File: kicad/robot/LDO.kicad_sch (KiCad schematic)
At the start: 17 parts, among them U14 MAX77642ANA+

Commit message: WARNING more BOM batch edits
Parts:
- R52: Manufacturer (none) -> Stackpole Electronics; Part Number (none) -> RMCF0603FT768K
- R53: Manufacturer (none) -> Panasonic; Part Number (none) -> ERJ-1GEF1133C
- R54: Manufacturer (none) -> Stackpole Electronics; Part Number (none) -> RMCF0603FT28K0
- R55: Manufacturer (none) -> Stackpole Electronics; Part Number (none) -> RMCF0603FT14K0
- U14: Part Number (none) -> MAX77642ANA+
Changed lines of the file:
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@@
     )
     (property "Description" "%1" (id 4) (at 72.39 121.92 0))
+    (property "Manufacturer" "Panasonic" (id 5) (at 68.58 118.11 0)
+      (effects (font (size 1.27 1.27)) hide)
+    )
+    (property "Part Number" "ERJ-1GEF1133C" (id 6) (at 68.58 118.11 0)
+      (effects (font (size 1.27 1.27)) hide)
+    )
     (pin "1")
     (pin "2")
@@
     (property "temperature range low" "-40°C" (id 30) (at 93.98 -5.08 0)
       (effects (font (size 1.27 1.27)) (justify left) hide)
+    )
+    (property "Part Number" "MAX77642ANA+" (id 31) (at 93.98 76.2 0)
+      (effects (font (size 1.27 1.27)) hide)
     )
     (pin "A1")
@@
     )
     (property "Description" "%1" (id 4) (at 82.55 121.92 0))
+    (property "Manufacturer" "Stackpole Electronics" (id 5) (at 78.74 118.11 0)
+      (effects (font (size 1.27 1.27)) hide)
+    )
+    (property "Part Number" "RMCF0603FT28K0" (id 6) (at 78.74 118.11 0)
+      (effects (font (size 1.27 1.27)) hide)
+    )
     (pin "1")
     (pin "2")
@@
     )
     (property "Description" "%1" (id 4) (at 92.71 121.92 0))
+    (property "Manufacturer" "Stackpole Electronics" (id 5) (at 88.9 118.11 0)
+      (effects (font (size 1.27 1.27)) hide)
+    )
+    (property "Part Number" "RMCF0603FT14K0" (id 6) (at 88.9 118.11 0)
+      (effects (font (size 1.27 1.27)) hide)
+    )
     (pin "1")
     (pin "2")
@@
     )
     (property "Description" "%1" (id 4) (at 62.23 121.92 0))
-    (pin "1")
-    (pin "2")
+    (property "Manufacturer" "Stackpole Electronics" (id 5) (at 58.42 118.11 0)
+      (effects (font (size 1.27 1.27)) hide)
+    )
+    (property "Part Number" "RMCF0603FT768K" (id 6) (at 58.42 118.11 0)
+      (effects (font (size 1.27 1.27)) hide)
+    )
+    (pin "1")
+    (pin "2")

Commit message: Added stock counts to parts I have
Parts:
- U14: Stock (none) -> 25
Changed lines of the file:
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@@
+      (effects (font (size 1.27 1.27)) hide)
+    )
+    (property "Stock" "25" (id 32) (at 93.98 76.2 0)
       (effects (font (size 1.27 1.27)) hide)
     )

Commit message: Batch BOM edits adding manufactuer and part numbers only
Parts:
- U14: Manufacturer (none) -> Maxim; manufacturer Maxim -> (none)
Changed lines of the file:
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@@
       (effects (font (size 1.27 1.27)) (justify left) hide)
     )
-    (property "manufacturer" "Maxim" (id 16) (at 93.98 30.48 0)
+    (property "manufacturer" "" (id 16) (at 93.98 30.48 0)
       (effects (font (size 1.27 1.27)) (justify left) hide)
     )
@@
       (effects (font (size 1.27 1.27)) hide)
     )
+    (property "Manufacturer" "Maxim" (id 33) (at 93.98 76.2 0)
+      (effects (font (size 1.27 1.27)) hide)
+    )

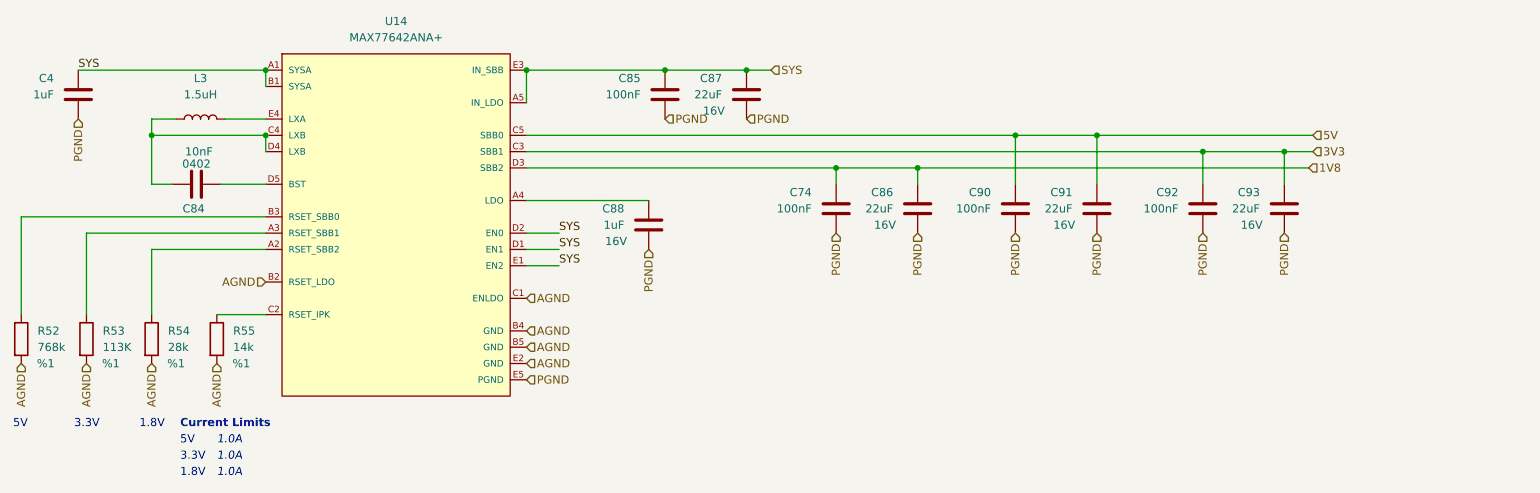
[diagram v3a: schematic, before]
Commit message: bulk BOM edits. Mainly dealing with cap voltage ratings and part selection
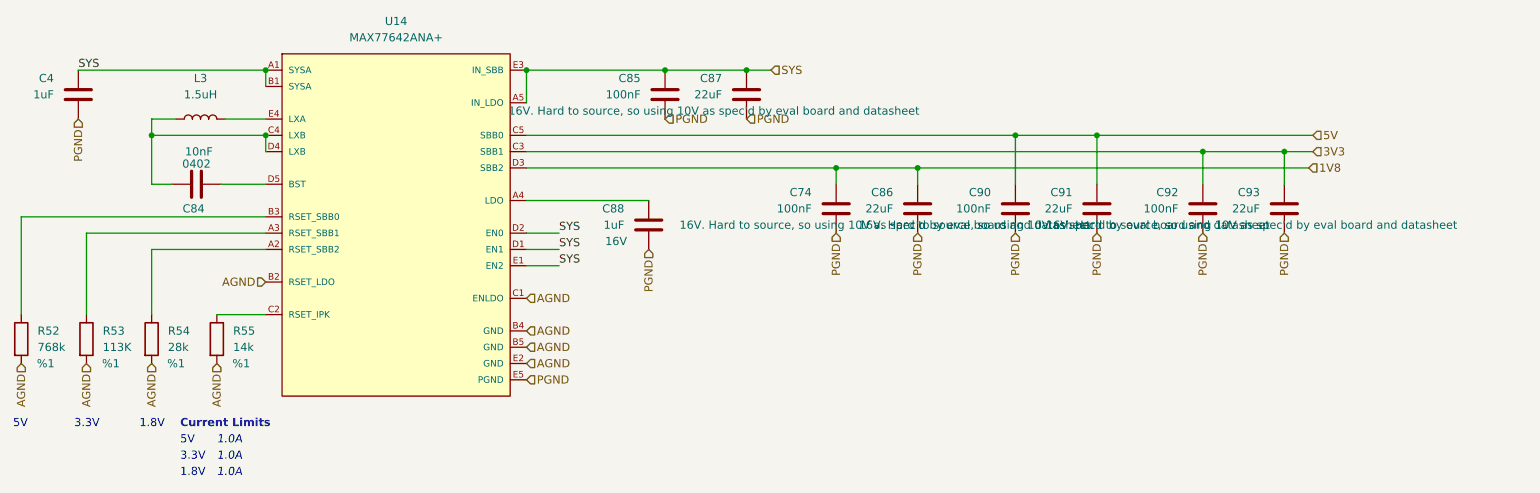
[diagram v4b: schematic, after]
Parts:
- C4: Manufacturer (none) -> Samsung; Part Number (none) -> CL10A105KQ8NNNC
- C74, C85, C90, C92: Manufacturer (none) -> Samsung; Part Number (none) -> CL10B104KB8NNWC
- C84: Manufacturer (none) -> Samsung; Part Number (none) -> CL05B103KA5NNNC
- C86, C87, C91, C93: Manufacturer (none) -> Samsung; Part Number (none) -> CL10A226MP8NUNE
- C88: Manufacturer (none) -> Samsung; Part Number (none) -> CL10A105KA8NNNC
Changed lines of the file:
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@@
       (effects (font (size 1.27 1.27)) hide)
     )
-    (property "Description" "16V" (id 4) (at 250.19 100.33 0))
+    (property "Description" "16V. Hard to source, so using 10V as spec'd by eval board and datasheet" (id 4) (at 250.19 100.33 0))
+    (property "Manufacturer" "Samsung" (id 5) (at 255.27 97.79 0)
+      (effects (font (size 1.27 1.27)) hide)
+    )
+    (property "Part Number" "CL10A226MP8NUNE" (id 6) (at 255.27 97.79 0)
+      (effects (font (size 1.27 1.27)) hide)
+    )
     (pin "1")
     (pin "2")
@@
     )
     (property "Description" "16V" (id 4) (at 151.13 102.87 0))
+    (property "Manufacturer" "Samsung" (id 5) (at 156.21 100.33 0)
+      (effects (font (size 1.27 1.27)) hide)
+    )
+    (property "Part Number" "CL10A105KA8NNNC" (id 6) (at 156.21 100.33 0)
+      (effects (font (size 1.27 1.27)) hide)
+    )
     (pin "1")
     (pin "2")
@@
       (effects (font (size 1.27 1.27)) hide)
     )
-    (property "Description" "16V" (id 4) (at 166.37 82.55 0))
+    (property "Description" "16V. Hard to source, so using 10V as spec'd by eval board and datasheet" (id 4) (at 166.37 82.55 0))
+    (property "Manufacturer" "Samsung" (id 5) (at 171.45 80.01 0)
+      (effects (font (size 1.27 1.27)) hide)
+    )
+    (property "Part Number" "CL10A226MP8NUNE" (id 6) (at 171.45 80.01 0)
+      (effects (font (size 1.27 1.27)) hide)
+    )
     (pin "1")
     (pin "2")
@@
       (effects (font (size 1.27 1.27)) hide)
     )
-    (property "Description" "16V" (id 4) (at 193.04 100.33 0))
+    (property "Description" "16V. Hard to source, so using 10V as spec'd by eval board and datasheet" (id 4) (at 193.04 100.33 0))
+    (property "Manufacturer" "Samsung" (id 5) (at 198.12 97.79 0)
+      (effects (font (size 1.27 1.27)) hide)
+    )
+    (property "Part Number" "CL10A226MP8NUNE" (id 6) (at 198.12 97.79 0)
+      (effects (font (size 1.27 1.27)) hide)
+    )
     (pin "1")
     (pin "2")
@@
     )
     (property "Description" "" (id 4) (at 180.34 100.33 0))
+    (property "Manufacturer" "Samsung" (id 5) (at 185.42 97.79 0)
+      (effects (font (size 1.27 1.27)) hide)
+    )
+    (property "Part Number" "CL10B104KB8NNWC" (id 6) (at 185.42 97.79 0)
+      (effects (font (size 1.27 1.27)) hide)
+    )
     (pin "1")
     (pin "2")
@@
     )
     (property "Description" "" (id 4) (at 153.67 82.55 0))
+    (property "Manufacturer" "Samsung" (id 5) (at 158.75 80.01 0)
+      (effects (font (size 1.27 1.27)) hide)
+    )
+    (property "Part Number" "CL10B104KB8NNWC" (id 6) (at 158.75 80.01 0)
+      (effects (font (size 1.27 1.27)) hide)
+    )
     (pin "1")
     (pin "2")
@@
     )
     (property "Description" "" (id 4) (at 62.23 82.55 0))
+    (property "Manufacturer" "Samsung" (id 5) (at 67.31 80.01 0)
+      (effects (font (size 1.27 1.27)) hide)
+    )
+    (property "Part Number" "CL10A105KQ8NNNC" (id 6) (at 67.31 80.01 0)
+      (effects (font (size 1.27 1.27)) hide)
+    )
     (pin "1")
     (pin "2")
@@
     )
     (property "Description" "" (id 4) (at 237.49 100.33 0))
+    (property "Manufacturer" "Samsung" (id 5) (at 242.57 97.79 0)
+      (effects (font (size 1.27 1.27)) hide)
+    )
+    (property "Part Number" "CL10B104KB8NNWC" (id 6) (at 242.57 97.79 0)
+      (effects (font (size 1.27 1.27)) hide)
+    )
     (pin "1")
     (pin "2")
@@
       (effects (font (size 1.27 1.27)) hide)
     )
-    (property "Description" "16V" (id 4) (at 220.98 100.33 0))
+    (property "Description" "16V. Hard to source, so using 10V as spec'd by eval board and datasheet" (id 4) (at 220.98 100.33 0))
+    (property "Manufacturer" "Samsung" (id 5) (at 226.06 97.79 0)
+      (effects (font (size 1.27 1.27)) hide)
+    )
+    (property "Part Number" "CL10A226MP8NUNE" (id 6) (at 226.06 97.79 0)
+      (effects (font (size 1.27 1.27)) hide)
+    )
     (pin "1")
     (pin "2")
@@
     )
     (property "Description" "" (id 4) (at 208.28 100.33 0))
+    (property "Manufacturer" "Samsung" (id 5) (at 213.36 97.79 0)
+      (effects (font (size 1.27 1.27)) hide)
+    )
+    (property "Part Number" "CL10B104KB8NNWC" (id 6) (at 213.36 97.79 0)
+      (effects (font (size 1.27 1.27)) hide)
+    )
     (pin "1")
     (pin "2")
@@
     )
     (property "Description" "0402" (id 4) (at 85.725 90.805 90))
-    (pin "1")
-    (pin "2")
+    (property "Manufacturer" "Samsung" (id 5) (at 85.725 93.98 0)
+      (effects (font (size 1.27 1.27)) hide)
+    )
+    (property "Part Number" "CL05B103KA5NNNC" (id 6) (at 85.725 93.98 0)
+      (effects (font (size 1.27 1.27)) hide)
+    )
+    (pin "1")
+    (pin "2")

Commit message: Bulk capacitor field edits
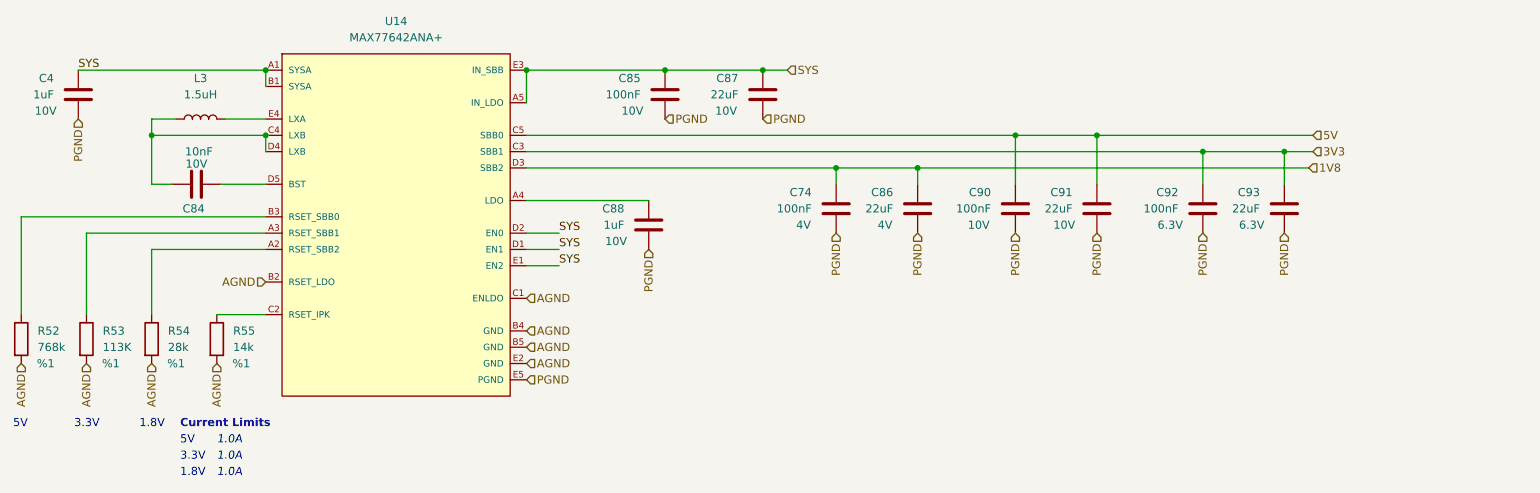
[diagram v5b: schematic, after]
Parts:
- C4: Manufacturer Samsung -> (none); Part Number CL10A105KQ8NNNC -> (none)
- C74, C85, C90, C92: Manufacturer Samsung -> (none); Part Number CL10B104KB8NNWC -> (none)
- C84: Manufacturer Samsung -> (none); Part Number CL05B103KA5NNNC -> (none)
- C86, C87, C91, C93: Manufacturer Samsung -> (none); Part Number CL10A226MP8NUNE -> (none)
- C88: Manufacturer Samsung -> (none); Part Number CL10A105KA8NNNC -> (none)
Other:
- moved on the sheet: C87
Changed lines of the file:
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@@
   (junction (at 242.57 88.9) (diameter 0) (color 0 0 0 0)
   )
-  (junction (at 171.45 76.2) (diameter 0) (color 0 0 0 0)
+  (junction (at 173.99 76.2) (diameter 0) (color 0 0 0 0)
   )
   (junction (at 158.75 76.2) (diameter 0) (color 0 0 0 0)
@@
     (stroke (width 0) (type default) (color 0 0 0 0))
   )
-  (wire (pts (xy 171.45 76.2) (xy 175.26 76.2))
+  (wire (pts (xy 173.99 76.2) (xy 177.8 76.2))
     (stroke (width 0) (type default) (color 0 0 0 0))
   )
@@
     (stroke (width 0) (type default) (color 0 0 0 0))
   )
-  (wire (pts (xy 158.75 76.2) (xy 171.45 76.2))
+  (wire (pts (xy 158.75 76.2) (xy 173.99 76.2))
     (stroke (width 0) (type default) (color 0 0 0 0))
   )
@@
     (effects (font (size 1.27 1.27)) (justify right))
   )
-  (hierarchical_label "PGND" (shape input) (at 171.45 83.82 0)
+  (hierarchical_label "PGND" (shape input) (at 173.99 83.82 0)
     (effects (font (size 1.27 1.27)) (justify left))
   )
@@
     (effects (font (size 1.27 1.27)) (justify left))
   )
-  (hierarchical_label "SYS" (shape input) (at 175.26 76.2 0)
+  (hierarchical_label "SYS" (shape input) (at 177.8 76.2 0)
     (effects (font (size 1.27 1.27)) (justify left))
   )
@@
       (effects (font (size 1.27 1.27)) hide)
     )
-    (property "Description" "16V. Hard to source, so using 10V as spec'd by eval board and datasheet" (id 4) (at 250.19 100.33 0))
-    (property "Manufacturer" "Samsung" (id 5) (at 255.27 97.79 0)
-      (effects (font (size 1.27 1.27)) hide)
-    )
-    (property "Part Number" "CL10A226MP8NUNE" (id 6) (at 255.27 97.79 0)
-      (effects (font (size 1.27 1.27)) hide)
-    )
+    (property "Description" "6.3V" (id 4) (at 250.19 100.33 0))
     (pin "1")
     (pin "2")
@@
       (effects (font (size 1.27 1.27)) hide)
     )
-    (property "Description" "16V" (id 4) (at 151.13 102.87 0))
-    (property "Manufacturer" "Samsung" (id 5) (at 156.21 100.33 0)
-      (effects (font (size 1.27 1.27)) hide)
-    )
-    (property "Part Number" "CL10A105KA8NNNC" (id 6) (at 156.21 100.33 0)
-      (effects (font (size 1.27 1.27)) hide)
-    )
-    (pin "1")
-    (pin "2")
-  )
-  (symbol (lib_id "Device:C") (at 171.45 80.01 0) (mirror y) (unit 1)
-    (in_bom yes) (on_board yes)
-    (property "Reference" "C87" (id 0) (at 167.64 77.4699 0)
-      (effects (font (size 1.27 1.27)) (justify left))
-    )
-    (property "Value" "22uF" (id 1) (at 167.64 80.0099 0)
-      (effects (font (size 1.27 1.27)) (justify left))
-    )
-    (property "Footprint" "Capacitor_SMD:C_0603_1608Metric" (id 2) (at 170.4848 83.82 0)
-      (effects (font (size 1.27 1.27)) hide)
-    )
-    (property "Datasheet" "~" (id 3) (at 171.45 80.01 0)
-      (effects (font (size 1.27 1.27)) hide)
-    )
-    (property "Description" "16V. Hard to source, so using 10V as spec'd by eval board and datasheet" (id 4) (at 166.37 82.55 0))
-    (property "Manufacturer" "Samsung" (id 5) (at 171.45 80.01 0)
-      (effects (font (size 1.27 1.27)) hide)
-    )
-    (property "Part Number" "CL10A226MP8NUNE" (id 6) (at 171.45 80.01 0)
-      (effects (font (size 1.27 1.27)) hide)
-    )
+    (property "Description" "10V" (id 4) (at 151.13 102.87 0))
+    (pin "1")
+    (pin "2")
+  )
+  (symbol (lib_id "Device:C") (at 173.99 80.01 0) (mirror y) (unit 1)
+    (in_bom yes) (on_board yes)
+    (property "Reference" "C87" (id 0) (at 170.18 77.4699 0)
+      (effects (font (size 1.27 1.27)) (justify left))
+    )
+    (property "Value" "22uF" (id 1) (at 170.18 80.0099 0)
+      (effects (font (size 1.27 1.27)) (justify left))
+    )
+    (property "Footprint" "Capacitor_SMD:C_0603_1608Metric" (id 2) (at 173.0248 83.82 0)
+      (effects (font (size 1.27 1.27)) hide)
+    )
+    (property "Datasheet" "~" (id 3) (at 173.99 80.01 0)
+      (effects (font (size 1.27 1.27)) hide)
+    )
+    (property "Description" "10V" (id 4) (at 168.275 82.55 0))
     (pin "1")
     (pin "2")
@@
       (effects (font (size 1.27 1.27)) hide)
     )
-    (property "Description" "16V. Hard to source, so using 10V as spec'd by eval board and datasheet" (id 4) (at 193.04 100.33 0))
-    (property "Manufacturer" "Samsung" (id 5) (at 198.12 97.79 0)
-      (effects (font (size 1.27 1.27)) hide)
-    )
-    (property "Part Number" "CL10A226MP8NUNE" (id 6) (at 198.12 97.79 0)
-      (effects (font (size 1.27 1.27)) hide)
-    )
+    (property "Description" "4V" (id 4) (at 193.04 100.33 0))
     (pin "1")
     (pin "2")
@@
       (effects (font (size 1.27 1.27)) hide)
     )
-    (property "Description" "" (id 4) (at 180.34 100.33 0))
-    (property "Manufacturer" "Samsung" (id 5) (at 185.42 97.79 0)
-      (effects (font (size 1.27 1.27)) hide)
-    )
-    (property "Part Number" "CL10B104KB8NNWC" (id 6) (at 185.42 97.79 0)
-      (effects (font (size 1.27 1.27)) hide)
-    )
+    (property "Description" "4V" (id 4) (at 180.34 100.33 0))
     (pin "1")
     (pin "2")
@@
       (effects (font (size 1.27 1.27)) hide)
     )
-    (property "Description" "" (id 4) (at 153.67 82.55 0))
-    (property "Manufacturer" "Samsung" (id 5) (at 158.75 80.01 0)
-      (effects (font (size 1.27 1.27)) hide)
-    )
-    (property "Part Number" "CL10B104KB8NNWC" (id 6) (at 158.75 80.01 0)
-      (effects (font (size 1.27 1.27)) hide)
-    )
+    (property "Description" "10V" (id 4) (at 153.67 82.55 0))
     (pin "1")
     (pin "2")
@@
       (effects (font (size 1.27 1.27)) hide)
     )
-    (property "Description" "" (id 4) (at 62.23 82.55 0))
-    (property "Manufacturer" "Samsung" (id 5) (at 67.31 80.01 0)
-      (effects (font (size 1.27 1.27)) hide)
-    )
-    (property "Part Number" "CL10A105KQ8NNNC" (id 6) (at 67.31 80.01 0)
-      (effects (font (size 1.27 1.27)) hide)
-    )
+    (property "Description" "10V" (id 4) (at 62.23 82.55 0))
     (pin "1")
     (pin "2")
@@
       (effects (font (size 1.27 1.27)) hide)
     )
-    (property "Description" "" (id 4) (at 237.49 100.33 0))
-    (property "Manufacturer" "Samsung" (id 5) (at 242.57 97.79 0)
-      (effects (font (size 1.27 1.27)) hide)
-    )
-    (property "Part Number" "CL10B104KB8NNWC" (id 6) (at 242.57 97.79 0)
-      (effects (font (size 1.27 1.27)) hide)
-    )
+    (property "Description" "6.3V" (id 4) (at 237.49 100.33 0))
     (pin "1")
     (pin "2")
@@
       (effects (font (size 1.27 1.27)) hide)
     )
-    (property "Description" "16V. Hard to source, so using 10V as spec'd by eval board and datasheet" (id 4) (at 220.98 100.33 0))
-    (property "Manufacturer" "Samsung" (id 5) (at 226.06 97.79 0)
-      (effects (font (size 1.27 1.27)) hide)
-    )
-    (property "Part Number" "CL10A226MP8NUNE" (id 6) (at 226.06 97.79 0)
-      (effects (font (size 1.27 1.27)) hide)
-    )
+    (property "Description" "10V" (id 4) (at 220.98 100.33 0))
     (pin "1")
     (pin "2")
@@
       (effects (font (size 1.27 1.27)) hide)
     )
-    (property "Description" "" (id 4) (at 208.28 100.33 0))
-    (property "Manufacturer" "Samsung" (id 5) (at 213.36 97.79 0)
-      (effects (font (size 1.27 1.27)) hide)
-    )
-    (property "Part Number" "CL10B104KB8NNWC" (id 6) (at 213.36 97.79 0)
-      (effects (font (size 1.27 1.27)) hide)
-    )
+    (property "Description" "10V" (id 4) (at 207.645 100.33 0))
     (pin "1")
     (pin "2")
@@
       (effects (font (size 1.27 1.27)) hide)
     )
-    (property "Description" "0402" (id 4) (at 85.725 90.805 90))
-    (property "Manufacturer" "Samsung" (id 5) (at 85.725 93.98 0)
-      (effects (font (size 1.27 1.27)) hide)
-    )
-    (property "Part Number" "CL05B103KA5NNNC" (id 6) (at 85.725 93.98 0)
-      (effects (font (size 1.27 1.27)) hide)
-    )
-    (pin "1")
-    (pin "2")
+    (property "Description" "10V" (id 4) (at 85.725 90.805 90))
+    (pin "1")
+    (pin "2")
